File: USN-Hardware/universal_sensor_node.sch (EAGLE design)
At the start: 26 parts, among them IC2 741G3157DCKR, IC3 AP2114, J2 USB-MICROB, U1 ATMEGA328P_TQFP

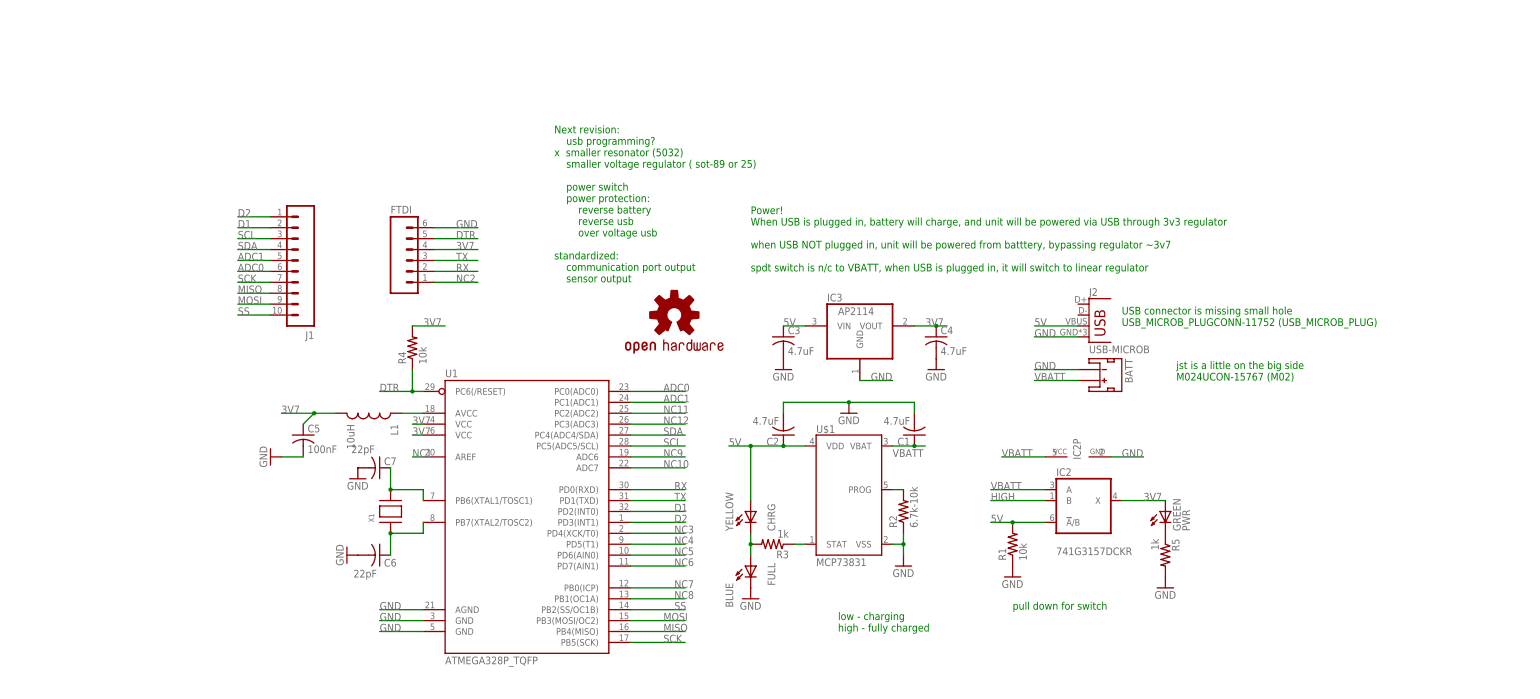
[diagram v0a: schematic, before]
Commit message: converting all parts into schematic library.
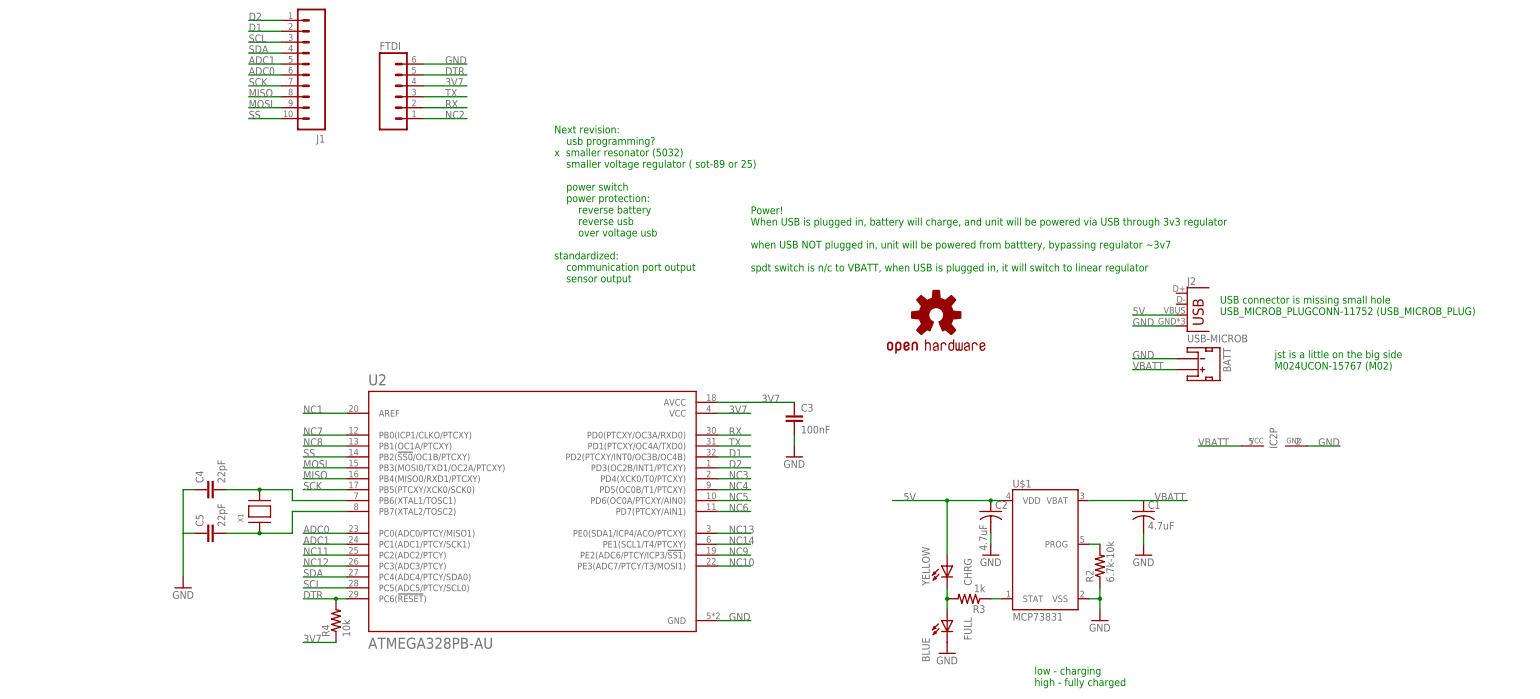
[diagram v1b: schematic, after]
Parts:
- removed C6, C7: 22pF, rcl:C-USC0603
- removed GREEN: PWR, led:LEDCHIPLED_0603
- removed IC3: AP2114, burr-brown:REG1117
- removed L1: 10uH, SparkFun-Passives:INDUCTOR30OHM,1.8A
- removed R1: 10k, rcl:R-US_R0603
- removed R5: 1k, rcl:R-US_R0603
- removed U1: ATMEGA328P_TQFP, SparkFun-DigitalIC:ATMEGA328P_TQFP
- added U2: ATMEGA328PB-AU, ATMEGA328PB-AU:ATMEGA328PB-AU
- C3: value 4.7uF -> 100nF; device rcl:C-USC1206 -> universal_sensor_node:100NF-50V-5%(0603)
- C4: value 4.7uF -> 22pF; device rcl:C-USC1206 -> universal_sensor_node:22PF-50V-5%(0603)
- C5: value 100nF -> 22pF; device rcl:C-USC0603 -> universal_sensor_node:22PF-50V-5%(0603)
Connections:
- removed net ASDF: L1.1, U1.AVCC
- removed net HIGH: IC2G$1.B
- removed net N$28: C7.1, U1.PB6(XTAL1/TOSC1), X1.P$2
- removed net N$29: C6.1, U1.PB7(XTAL2/TOSC2), X1.P$1
- removed net N$5: GREEN.C, R5.1
- new net N$26: C4.2, U2.PB6(XTAL1/TOSC1), X1.P$2
- new net N$27: C5.2, U2.PB7(XTAL2/TOSC2), X1.P$1
- new net NC13: U2.PE0(SDA1/ICP4/ACO/PTCXY)
- new net NC14: U2.PE1(SCL1/T4/PTCXY)
- net 3V7: now also C3.1, R4.1, U2.AVCC, U2.VCC; no longer C4.1, C5.1, GREEN.A, IC2G$1.X, IC3.VOUT, L1.2, R4.2, U1.VCC@4, U1.VCC@6
- net 5V: no longer C3.1, IC2G$1.!A!/B, IC3.VIN, R1.2
- net ADC0: now also U2.PC0(ADC0/PTCY/MISO1); no longer U1.PC0(ADC0)
- net ADC1: now also U2.PC1(ADC1/PTCY/SCK1); no longer U1.PC1(ADC1)
- net D1: now also U2.PD2(PTCXY/INT0/OC3B/OC4B); no longer U1.PD2(INT0)
- net D2: now also U2.PD3(OC2B/INT1/PTCXY); no longer U1.PD3(INT1)
- net DTR: now also R4.2, U2.PC6(!RESET!); no longer R4.1, U1.PC6(/RESET)
- net GND: now also C4.1, C5.1, U2.GND; no longer C4.2, C5.2, C6.2, C7.2, IC3.GND, R1.1, R5.2, U1.AGND, U1.GND@3, U1.GND@5
- net MISO: now also U2.PB4(MISO0/RXD1/PTCXY); no longer U1.PB4(MISO)
- net MOSI: now also U2.PB3(MOSI0/TXD1/OC2A/PTCXY); no longer U1.PB3(MOSI/OC2)
- net NC1: now also U2.AREF; no longer U1.AREF
- net NC10: now also U2.PE3(ADC7/PTCY/T3/MOSI1); no longer U1.ADC7
- net NC11: now also U2.PC2(ADC2/PTCY); no longer U1.PC2(ADC2)
- net NC12: now also U2.PC3(ADC3/PTCY); no longer U1.PC3(ADC3)
- net NC3: now also U2.PD4(XCK0/T0/PTCXY); no longer U1.PD4(XCK/T0)
- net NC4: now also U2.PD5(OC0B/T1/PTCXY); no longer U1.PD5(T1)
- net NC5: now also U2.PD6(OC0A/PTCXY/AIN0); no longer U1.PD6(AIN0)
- net NC6: now also U2.PD7(PTCXY/AIN1); no longer U1.PD7(AIN1)
- net NC7: now also U2.PB0(ICP1/CLKO/PTCXY); no longer U1.PB0(ICP)
- net NC8: now also U2.PB1(OC1A/PTCXY); no longer U1.PB1(OC1A)
- net NC9: now also U2.PE2(ADC6/PTCY/ICP3/!SS1!); no longer U1.ADC6
- net RX: now also U2.PD0(PTCXY/OC3A/RXD0); no longer U1.PD0(RXD)
- net SCK: now also U2.PB5(PTCXY/XCK0/SCK0); no longer U1.PB5(SCK)
- net SCL: now also U2.PC5(ADC5/PTCY/SCL0); no longer U1.PC5(ADC5/SCL)
- net SDA: now also U2.PC4(ADC4/PTCY/SDA0); no longer U1.PC4(ADC4/SDA)
- net SS: now also U2.PB2(!SS0!/OC1B/PTCXY); no longer U1.PB2(SS/OC1B)
- net TX: now also U2.PD1(PTCXY/OC4A/TXD0); no longer U1.PD1(TXD)
- net VBATT: no longer IC2G$1.A
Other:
- note removed: "pull down for switch"
- moved on the sheet: BATT, BLUE, C1, C2, C3, C4, C5, FTDI, IC2P, J1, J2, R2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

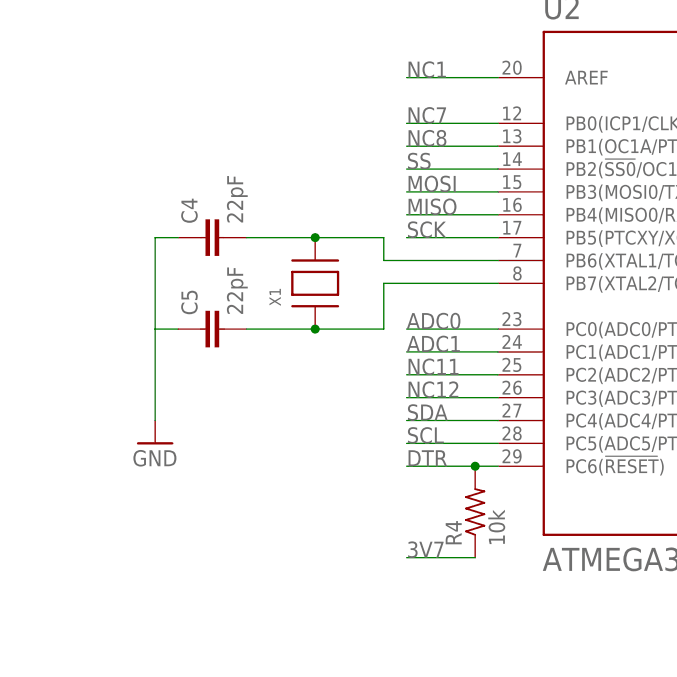
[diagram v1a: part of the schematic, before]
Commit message: finished with atmega components transfer.
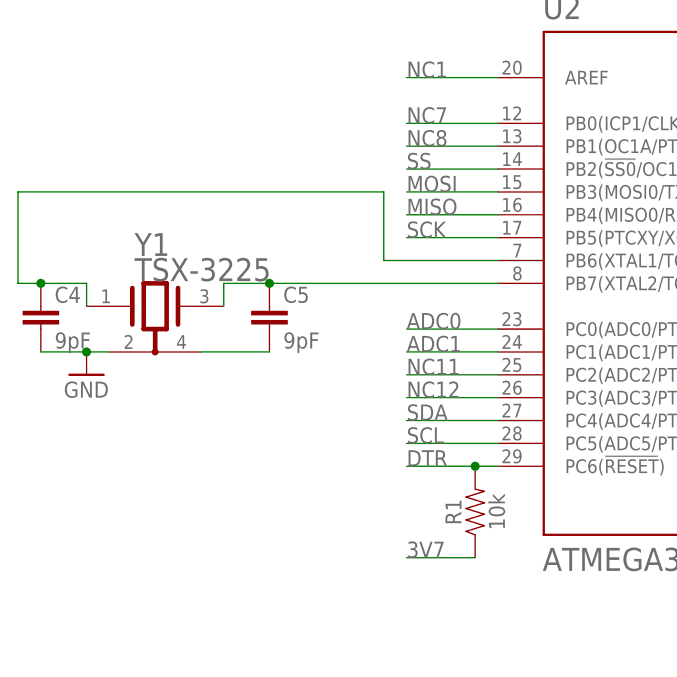
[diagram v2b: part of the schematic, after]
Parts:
- removed R4: 10k, rcl:R-US_R0603
- removed X1: (no value), adafruit:XTALNX5032
- added R1: 10k, universal_sensor_node:RES_0603_10K_1%_.1W-0603-1/10W-1%
- added Y1: TSX-3225EPSON_TSX-3225_16.0000MF09Z-AC3_0_0, universal_sensor_node:TSX-3225EPSON_TSX-3225_16.0000MF09Z-AC3_0_0
- C4, C5: value 22pF -> 9pF; device universal_sensor_node:22PF-50V-5%(0603) -> universal_sensor_node:9PF-50V(0603)
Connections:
- new net N$4: C5.2, Y1.2_GND
- net 3V7: now also R1.1; no longer R4.1
- net DTR: now also R1.2; no longer R4.2
- net GND: now also C4.2, Y1.1_GND; no longer C4.1, C5.1
- net N$26: now also C4.1, Y1.1; no longer C4.2, X1.P$2
- net N$27: now also C5.1, Y1.3; no longer C5.2, X1.P$1
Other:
- moved on the sheet: C4, C5
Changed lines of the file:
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@@
 <part name="J2" library="SparkFun-Connectors" deviceset="USB" device="-MICROB"/>
 <part name="LOGO1" library="SparkFun-Aesthetics" deviceset="OSHW-LOGO" device="MINI"/>
-<part name="X1" library="adafruit" deviceset="XTAL" device="NX5032"/>
 <part name="U2" library="ATMEGA328PB-AU" deviceset="ATMEGA328PB-AU" device=""/>
 <part name="GND1" library="supply1" deviceset="GND" device=""/>
-<part name="R4" library="rcl" deviceset="R-US_" device="R0603" value="10k"/>
 <part name="C3" library="universal_sensor_node" deviceset="100NF-50V-5%(0603)" device="" value="100nF"/>
-<part name="C4" library="universal_sensor_node" deviceset="22PF-50V-5%(0603)" device="" value="22pF"/>
-<part name="C5" library="universal_sensor_node" deviceset="22PF-50V-5%(0603)" device="" value="22pF"/>
+<part name="Y1" library="universal_sensor_node" deviceset="TSX-3225" device="EPSON_TSX-3225_16.0000MF09Z-AC3_0_0"/>
+<part name="C4" library="universal_sensor_node" deviceset="9PF-50V(0603)" device="" value="9pF"/>
+<part name="C5" library="universal_sensor_node" deviceset="9PF-50V(0603)" device="" value="9pF"/>
+<part name="R1" library="universal_sensor_node" deviceset="RES_0603_10K_1%_.1W" device="-0603-1/10W-1%" value="10k"/>
 </parts>
 <sheets>
@@
 <attribute name="VALUE" x="127" y="53.34" size="1.778" layer="96"/>
 </instance>
-<instance part="GND8" gate="1" x="-12.7" y="25.4" smashed="yes">
-<attribute name="VALUE" x="-15.24" y="22.86" size="1.778" layer="96"/>
+<instance part="GND8" gate="1" x="-20.32" y="33.02" smashed="yes">
+<attribute name="VALUE" x="-22.86" y="30.48" size="1.778" layer="96"/>
 </instance>
 <instance part="BATT" gate="G$1" x="223.52" y="78.74" smashed="yes" rot="R270">
@@
 </instance>
 <instance part="LOGO1" gate="G$1" x="162.56" y="88.9" smashed="yes"/>
-<instance part="X1" gate="G$1" x="5.08" y="43.18" smashed="yes" rot="R90">
-<attribute name="NAME" x="1.27" y="40.64" size="1.27" layer="95" font="vector" rot="R90"/>
-<attribute name="VALUE" x="10.16" y="39.37" size="1.27" layer="96" font="vector" rot="R90"/>
-</instance>
 <instance part="U2" gate="G$1" x="68.58" y="43.18" smashed="yes">
 <attribute name="NAME" x="30.365" y="72.5428" size="2.55326875" layer="95"/>
@@
 <attribute name="VALUE" x="208.28" y="30.48" size="1.778" layer="96"/>
 </instance>
-<instance part="R4" gate="G$1" x="22.86" y="17.78" smashed="yes" rot="R90">
-<attribute name="NAME" x="21.3614" y="13.97" size="1.778" layer="95" rot="R90"/>
-<attribute name="VALUE" x="26.162" y="13.97" size="1.778" layer="96" rot="R90"/>
-</instance>
 <instance part="C3" gate="G$1" x="129.54" y="63.5" smashed="yes">
 <attribute name="NAME" x="131.064" y="66.421" size="1.778" layer="95"/>
 <attribute name="VALUE" x="131.064" y="61.341" size="1.778" layer="96"/>
 </instance>
-<instance part="C4" gate="G$1" x="-5.08" y="48.26" smashed="yes" rot="R90">
-<attribute name="NAME" x="-8.001" y="49.784" size="1.778" layer="95" rot="R90"/>
-<attribute name="VALUE" x="-2.921" y="49.784" size="1.778" layer="96" rot="R90"/>
-</instance>
-<instance part="C5" gate="G$1" x="-5.08" y="38.1" smashed="yes" rot="R90">
-<attribute name="NAME" x="-8.001" y="39.624" size="1.778" layer="95" rot="R90"/>
-<attribute name="VALUE" x="-2.921" y="39.624" size="1.778" layer="96" rot="R90"/>
+<instance part="Y1" gate="G$0" x="-17.78" y="48.26" smashed="yes">
+<attribute name="NAME" x="-14.986" y="48.768" size="2.54" layer="95" align="top-left"/>
+</instance>
+<instance part="C4" gate="G$1" x="-25.4" y="38.1" smashed="yes">
+<attribute name="NAME" x="-23.876" y="41.021" size="1.778" layer="95"/>
+<attribute name="VALUE" x="-23.876" y="35.941" size="1.778" layer="96"/>
+</instance>
+<instance part="C5" gate="G$1" x="0" y="38.1" smashed="yes">
+<attribute name="NAME" x="1.524" y="41.021" size="1.778" layer="95"/>
+<attribute name="VALUE" x="1.524" y="35.941" size="1.778" layer="96"/>
+</instance>
+<instance part="R1" gate="G$1" x="22.86" y="17.78" smashed="yes" rot="R90">
+<attribute name="NAME" x="21.336" y="17.78" size="1.778" layer="95" font="vector" rot="R90" align="bottom-center"/>
+<attribute name="VALUE" x="24.384" y="17.78" size="1.778" layer="96" font="vector" rot="R90" align="top-center"/>
 </instance>
 </instances>
@@
 <pinref part="U2" gate="G$1" pin="PC6(!RESET!)"/>
 <label x="15.24" y="22.86" size="1.778" layer="95"/>
-<pinref part="R4" gate="G$1" pin="2"/>
+<pinref part="R1" gate="G$1" pin="2"/>
 <wire x1="22.86" y1="22.86" x2="25.4" y2="22.86" width="0.1524" layer="91"/>
 <junction x="22.86" y="22.86"/>
@@
 <wire x1="15.24" y1="12.7" x2="22.86" y2="12.7" width="0.1524" layer="91"/>
 <label x="15.24" y="12.7" size="1.778" layer="95"/>
-<pinref part="R4" gate="G$1" pin="1"/>
+<pinref part="R1" gate="G$1" pin="1"/>
 </segment>
 <segment>
@@
 </segment>
 <segment>
-<pinref part="GND8" gate="1" pin="GND"/>
-<wire x1="-10.16" y1="38.1" x2="-12.7" y2="38.1" width="0.1524" layer="91"/>
-<wire x1="-12.7" y1="38.1" x2="-12.7" y2="27.94" width="0.1524" layer="91"/>
-<wire x1="-10.16" y1="48.26" x2="-12.7" y2="48.26" width="0.1524" layer="91"/>
-<wire x1="-12.7" y1="48.26" x2="-12.7" y2="38.1" width="0.1524" layer="91"/>
-<pinref part="C4" gate="G$1" pin="1"/>
-<pinref part="C5" gate="G$1" pin="1"/>
-</segment>
-<segment>
 <pinref part="J2" gate="G$1" pin="GND"/>
 <wire x1="218.44" y1="86.36" x2="208.28" y2="86.36" width="0.1524" layer="91"/>
@@
 <pinref part="U2" gate="G$1" pin="GND"/>
 <label x="114.3" y="17.78" size="1.778" layer="95"/>
+</segment>
+<segment>
+<pinref part="C4" gate="G$1" pin="2"/>
+<pinref part="Y1" gate="G$0" pin="1_GND"/>
+<wire x1="-25.4" y1="35.56" x2="-20.32" y2="35.56" width="0.1524" layer="91"/>
+<pinref part="GND8" gate="1" pin="GND"/>
+<wire x1="-20.32" y1="35.56" x2="-17.78" y2="35.56" width="0.1524" layer="91"/>
+<junction x="-20.32" y="35.56"/>
 </segment>
 </net>
@@
 <wire x1="12.7" y1="45.72" x2="25.4" y2="45.72" width="0.1524" layer="91"/>
 <pinref part="U2" gate="G$1" pin="PB6(XTAL1/TOSC1)"/>
-<wire x1="12.7" y1="45.72" x2="12.7" y2="48.26" width="0.1524" layer="91"/>
-<wire x1="12.7" y1="48.26" x2="5.08" y2="48.26" width="0.1524" layer="91"/>
-<wire x1="-2.54" y1="48.26" x2="5.08" y2="48.26" width="0.1524" layer="91"/>
-<pinref part="X1" gate="G$1" pin="P$2"/>
-<junction x="5.08" y="48.26"/>
-<pinref part="C4" gate="G$1" pin="2"/>
+<wire x1="12.7" y1="45.72" x2="12.7" y2="53.34" width="0.1524" layer="91"/>
+<wire x1="12.7" y1="53.34" x2="-27.94" y2="53.34" width="0.1524" layer="91"/>
+<wire x1="-27.94" y1="53.34" x2="-27.94" y2="43.18" width="0.1524" layer="91"/>
+<pinref part="Y1" gate="G$0" pin="1"/>
+<wire x1="-27.94" y1="43.18" x2="-25.4" y2="43.18" width="0.1524" layer="91"/>
+<pinref part="C4" gate="G$1" pin="1"/>
+<wire x1="-25.4" y1="43.18" x2="-20.32" y2="43.18" width="0.1524" layer="91"/>
+<wire x1="-20.32" y1="43.18" x2="-20.32" y2="40.64" width="0.1524" layer="91"/>
+<junction x="-25.4" y="43.18"/>
 </segment>
 </net>
 <net name="N$27" class="0">
 <segment>
-<wire x1="12.7" y1="43.18" x2="25.4" y2="43.18" width="0.1524" layer="91"/>
 <pinref part="U2" gate="G$1" pin="PB7(XTAL2/TOSC2)"/>
-<wire x1="12.7" y1="38.1" x2="5.08" y2="38.1" width="0.1524" layer="91"/>
-<wire x1="-2.54" y1="38.1" x2="5.08" y2="38.1" width="0.1524" layer="91"/>
-<pinref part="X1" gate="G$1" pin="P$1"/>
-<junction x="5.08" y="38.1"/>
-<wire x1="12.7" y1="43.18" x2="12.7" y2="38.1" width="0.1524" layer="91"/>
+<wire x1="-5.08" y1="40.64" x2="-5.08" y2="43.18" width="0.1524" layer="91"/>
+<wire x1="-5.08" y1="43.18" x2="0" y2="43.18" width="0.1524" layer="91"/>
+<pinref part="Y1" gate="G$0" pin="3"/>
+<pinref part="C5" gate="G$1" pin="1"/>
+<wire x1="0" y1="43.18" x2="25.4" y2="43.18" width="0.1524" layer="91"/>
+<junction x="0" y="43.18"/>
+</segment>
+</net>
+<net name="N$4" class="0">
+<segment>
+<pinref part="Y1" gate="G$0" pin="2_GND"/>
 <pinref part="C5" gate="G$1" pin="2"/>
-</segment>
-</net>
+<wire x1="-7.62" y1="35.56" x2="0" y2="35.56" width="0.1524" layer="91"/>
+</segment>
+</net>
